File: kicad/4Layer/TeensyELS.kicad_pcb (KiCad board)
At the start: 4 copper layers, 96 x 85 mm, 47 parts, among them J1 RJ45_Shielded, J2 Conn_01x04_Pin, J3 Conn_01x04_Pin, J4 Screw_Terminal_01x02, Q1 BSS138, Q2 BSS138, Q3 BSS138, Q4 BSS138, Q5 BSS138, Q6 BSS138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

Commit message: Updated board version
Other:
- board text added: "TeensyELS v0.4"
- board text removed: "TeensyELS v0.3"
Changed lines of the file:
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@@
 		(layer "Edge.Cuts")
 	)
-	(gr_text "TeensyELS v0.3"
+	(gr_text "TeensyELS v0.4"
 		(at 48 28 0)
 		(layer "B.SilkS")
@@
 		)
 	)
-	(gr_text "TeensyELS v0.3"
+	(gr_text "TeensyELS v0.4\n"
 		(at 21.5 28 0)
 		(layer "F.SilkS")

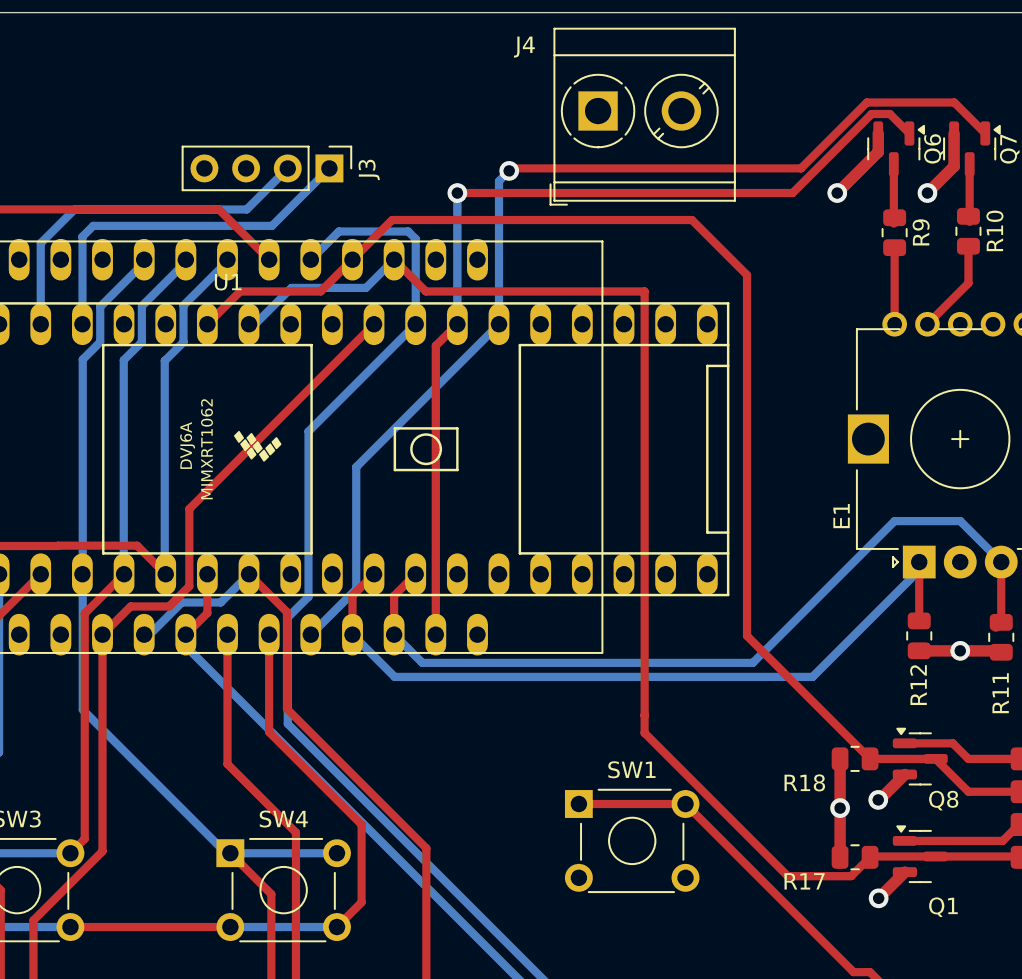
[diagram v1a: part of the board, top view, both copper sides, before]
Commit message: Fix  incorrect pin usage
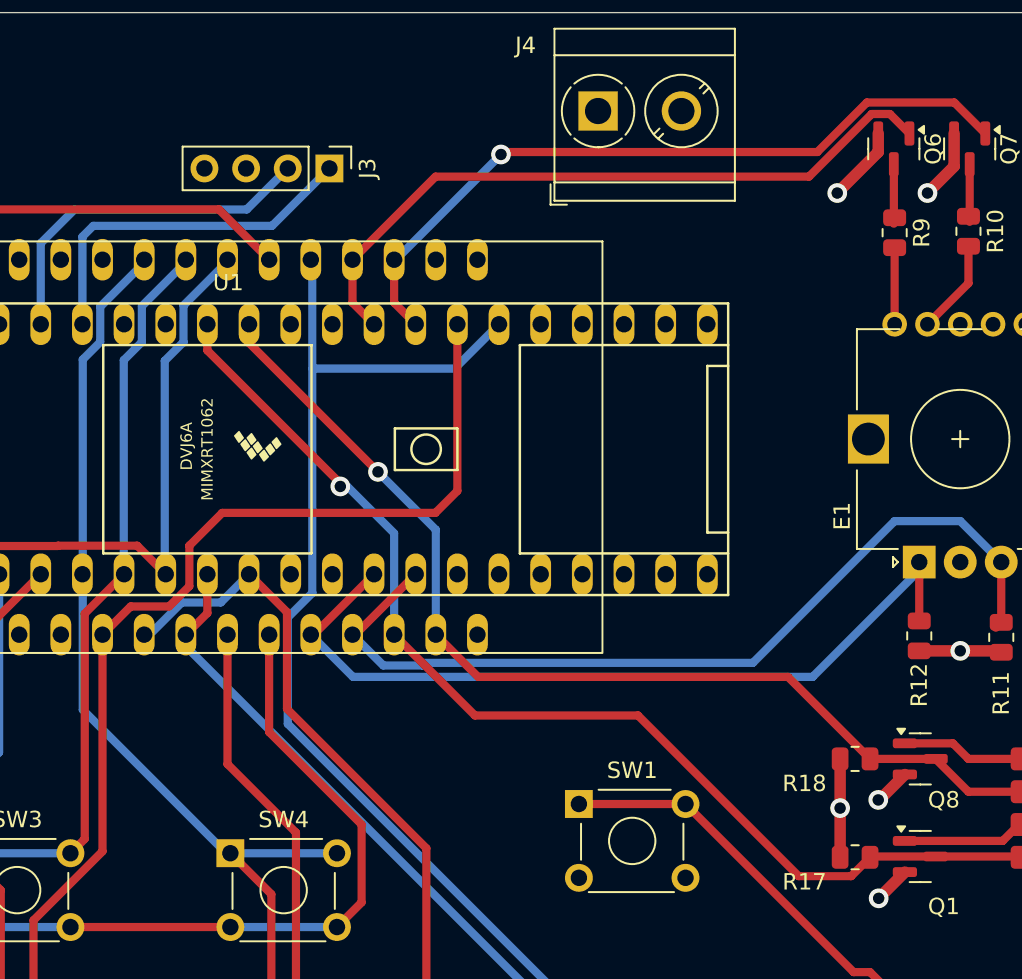
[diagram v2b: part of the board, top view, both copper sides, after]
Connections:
- MCU1 pad 10: /UIEncB -> /EncB
- MCU1 pad 11: /Red -> /EncA
- MCU1 pad 21: /EncA -> /Red
- MCU1 pad 22: /EncB -> /Green
- MCU1 pad 8: /Green -> /UIEncA
- MCU1 pad 9: /UIEncA -> /UIEncB
- U1 pad 30: /Green -> /Ena
- U1 pad 31: /Red -> /Alm
- U1 pad 32: /Ena -> /Green
- U1 pad 33: /Alm -> /Red
- U1 pad 36: /EncB -> /EncA
- U1 pad 37: /EncA -> /EncB
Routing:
- net /Green: track 64.8 -> 45.3 mm
- net /EncA: track 79.4 -> 63.2 mm, vias 0 -> 1
- net /Red: track 57.5 -> 42.6 mm, vias 1 -> 0
- net /EncB: track 80.4 -> 68.6 mm, vias 0 -> 1
- net /Alm: track 104.1 -> 113.8 mm
- net /UIEncB: track 50.7 -> 54.6 mm
- net /UIEncA: track 46.6 -> 50.3 mm
- net /Ena: track 89.1 -> 90.5 mm
- net +5V: track 266.0 -> 265.4 mm

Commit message: Updated board design to fix incorrect pin usage
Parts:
- R15, R16, R17: value 10K -> 1K
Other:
- board text added: "TeensyELS v0.5"
- board text removed: "TeensyELS v0.4"
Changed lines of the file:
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@@
 			)
 		)
-		(property "Value" "10K"
+		(property "Value" "1K"
 			(at 0 1.65 0)
 			(layer "F.Fab")
@@
 			)
 		)
-		(property "Value" "10K"
+		(property "Value" "1K"
 			(at 0 1.65 0)
 			(layer "F.Fab")
@@
 			)
 		)
-		(property "Value" "10K"
+		(property "Value" "1K"
 			(at 0 1.65 0)
 			(layer "F.Fab")
@@
 		(layer "Edge.Cuts")
 	)
-	(gr_text "TeensyELS v0.4"
+	(gr_text "TeensyELS v0.5"
 		(at 48 28 0)
 		(layer "B.SilkS")
@@
 		)
 	)
-	(gr_text "TeensyELS v0.4\n"
+	(gr_text "TeensyELS v0.5\n"
 		(at 21.5 28 0)
 		(layer "F.SilkS")
